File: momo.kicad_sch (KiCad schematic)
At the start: 98 parts, among them J1 USB C, SW1 MX_SW_HS, SW10 MX_SW_HS, SW11 MX_SW_HS, SW12 MX_SW_HS, SW13 MX_SW_HS, SW14 MX_SW_HS, SW15 MX_SW_HS, SW16 MX_SW_HS, SW17 MX_SW_HS, SW18 MX_SW_HS, SW19 MX_SW_HS, SW2 MX_SW_HS, SW20 MX_SW_HS, SW21 MX_SW_HS, SW22 MX_SW_HS, SW23 MX_SW_HS, SW24 MX_SW_HS, SW25 MX_SW_HS, SW26 MX_SW_HS, SW27 MX_SW_HS, SW28 MX_SW_HS, SW29 MX_SW_HS, SW3 MX_SW_HS, SW30 MX_SW_HS, SW31 MX_SW_HS, SW32 MX_SW_HS, SW33 MX_SW_HS, SW34 MX_SW_HS, SW35 MX_SW_HS, SW36 MX_SW_HS, SW37 MX_SW_HS, SW38 MX_SW_HS, SW39 MX_SW_HS, SW4 MX_SW_HS, SW40 MX_SW_HS, SW41 MX_SW_HS, SW42 MX_SW_HS, SW43 MX_SW_HS, SW44 MX_SW_HS, SW45 MX_SW_HS, SW46 MX_SW_HS, SW47 MX_SW_HS, SW48 MX_SW_HS, SW5 MX_SW_HS, SW6 MX_SW_HS, SW7 MX_SW_HS, SW8 MX_SW_HS, SW9 MX_SW_HS, U1 WeAct-RP2040-Pico

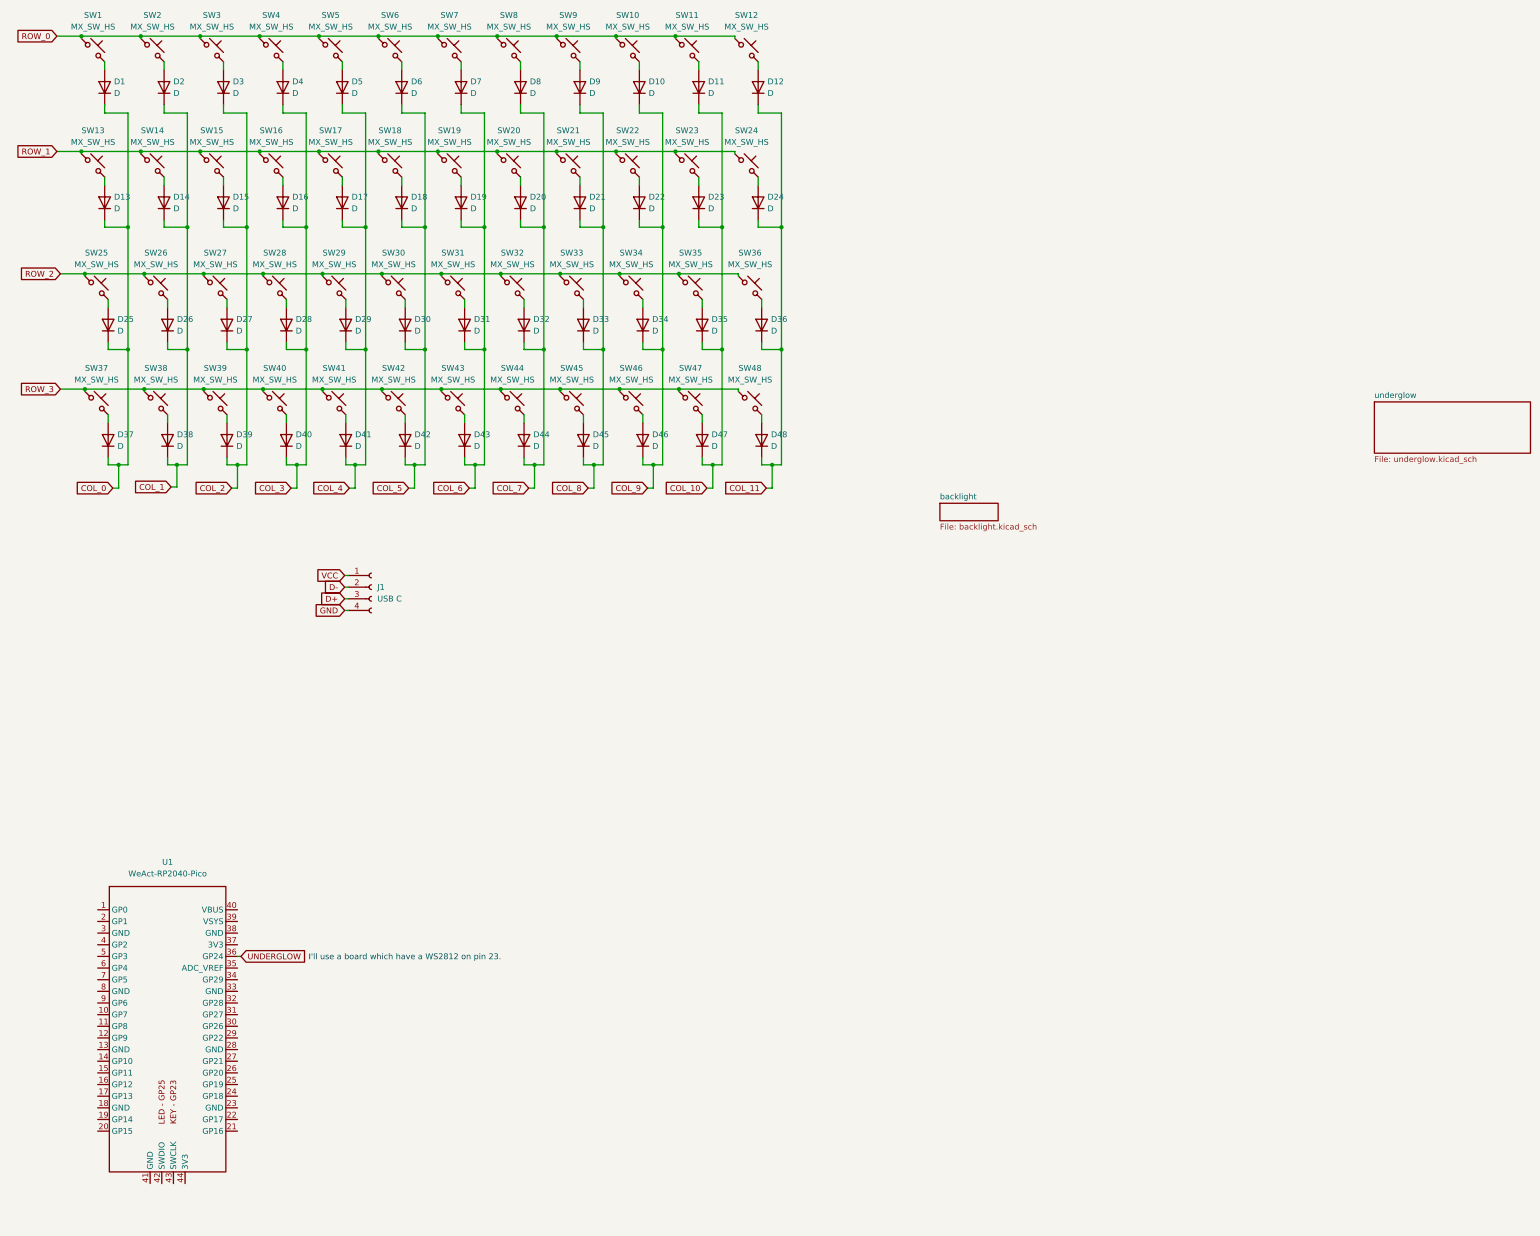
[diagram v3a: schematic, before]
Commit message: Added i2c pins
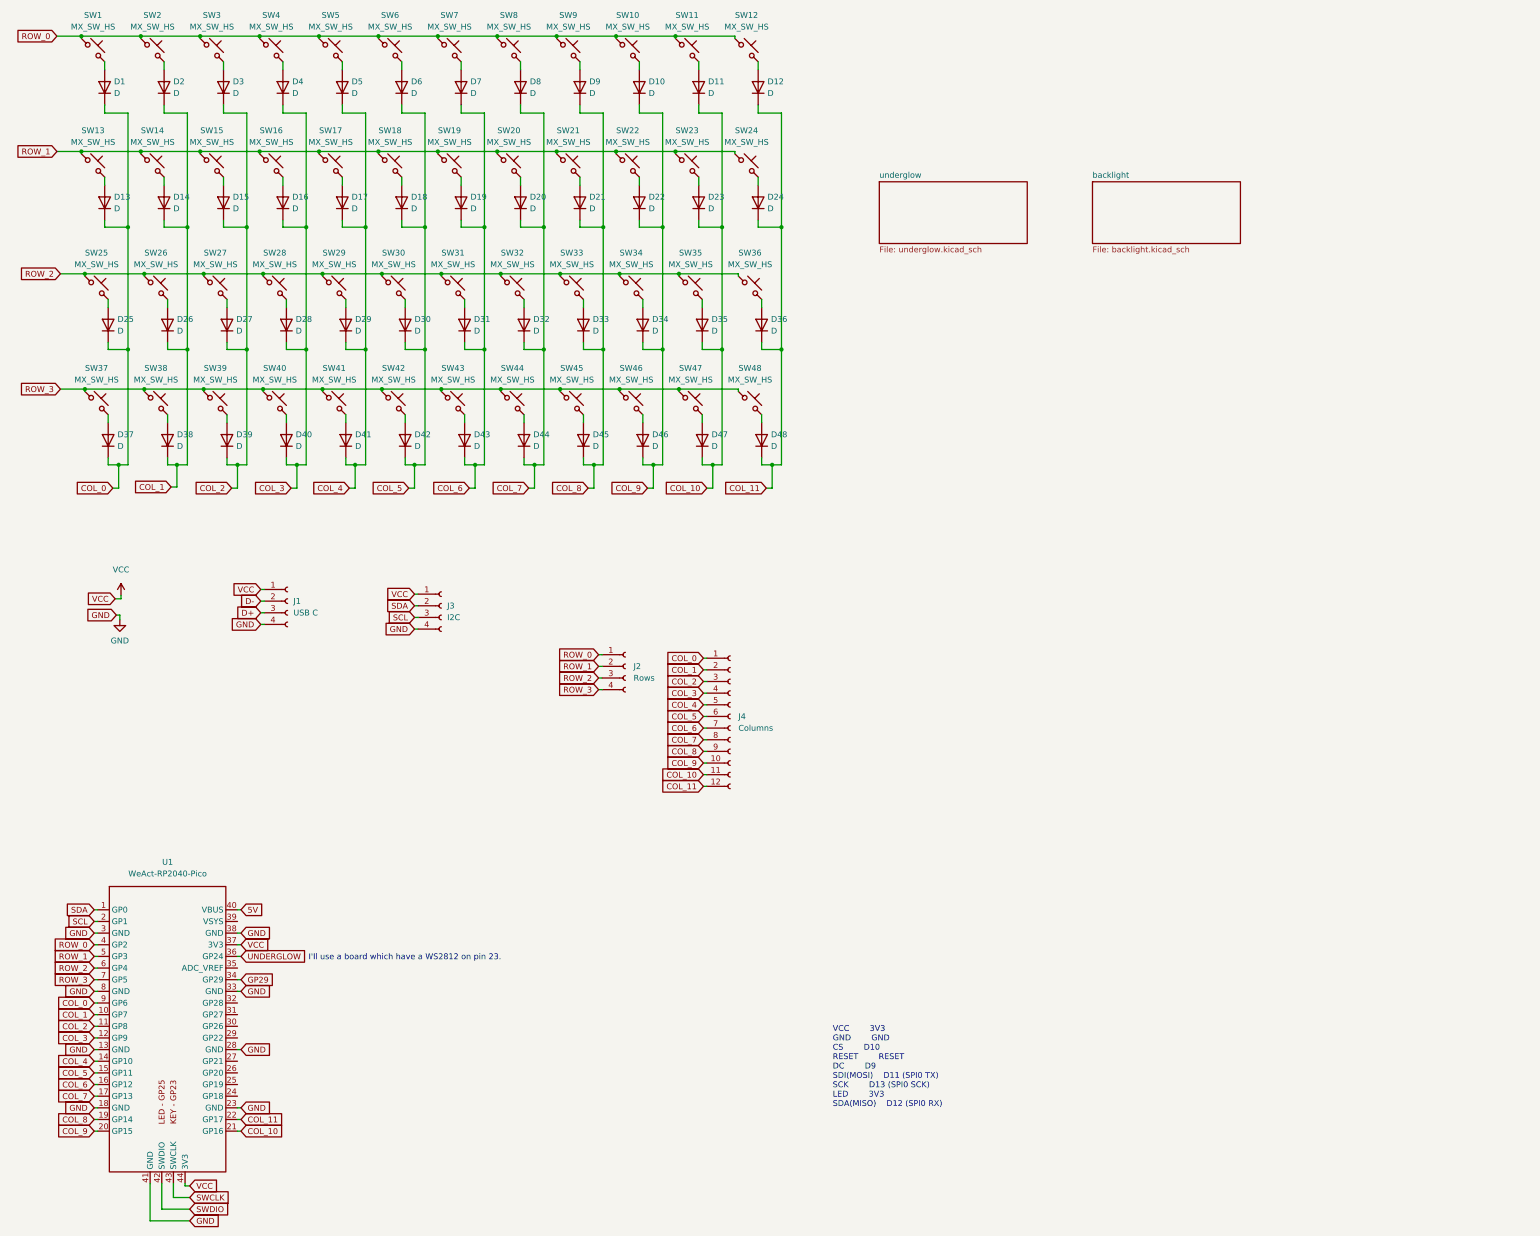
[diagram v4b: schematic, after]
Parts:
- added J2: Rows, Connector_PinHeader_2.54mm:PinHeader_1x04_P2.54mm_Vertical, symbol Connector:Conn_01x04_Female
- added J3: I2C, Connector_PinHeader_2.54mm:PinHeader_1x04_P2.54mm_Vertical, symbol Connector:Conn_01x04_Female
- added J4: Columns, Connector_PinHeader_2.54mm:PinHeader_1x12_P2.54mm_Vertical, symbol Connector:Conn_01x12_Female
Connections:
- net COL_0: now also U1.9 (GP6), J4.1 (Pin_1)
- net COL_1: now also U1.10 (GP7), J4.2 (Pin_2)
- net COL_10: now also U1.21 (GP16), J4.11 (Pin_11)
- net COL_11: now also U1.22 (GP17), J4.12 (Pin_12)
- net COL_2: now also U1.11 (GP8), J4.3 (Pin_3)
- net COL_3: now also U1.12 (GP9), J4.4 (Pin_4)
- net COL_4: now also U1.14 (GP10), J4.5 (Pin_5)
- net COL_5: now also U1.15 (GP11), J4.6 (Pin_6)
- net COL_6: now also U1.16 (GP12), J4.7 (Pin_7)
- net COL_7: now also U1.17 (GP13), J4.8 (Pin_8)
- net COL_8: now also U1.19 (GP14), J4.9 (Pin_9)
- net COL_9: now also U1.20 (GP15), J4.10 (Pin_10)
- net GND: now also U1.13 (GND), U1.18 (GND), U1.23 (GND), U1.28 (GND), U1.3 (GND), U1.33 (GND), U1.38 (GND), U1.41 (GND), U1.8 (GND), J3.4 (Pin_4)
- net ROW_0: now also U1.4 (GP2), J2.1 (Pin_1)
- net ROW_1: now also U1.5 (GP3), J2.2 (Pin_2)
- net ROW_2: now also U1.6 (GP4), J2.3 (Pin_3)
- net ROW_3: now also U1.7 (GP5), J2.4 (Pin_4)
- net VCC: now also U1.37 (3V3), U1.44 (3V3), J3.1 (Pin_1)
- net SDA: now reaches U1.1 (GP0)
- net SDA: now also J3.2 (Pin_2)
- net SCL: now reaches U1.2 (GP1)
- net SCL: now also J3.3 (Pin_3)
- net GP29: now reaches U1.34 (GP29)
- net 5V: now reaches U1.40 (VBUS)
- net SWDIO: now reaches U1.42 (SWDIO)
- net SWCLK: now reaches U1.43 (SWCLK)
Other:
- note added: "VCC 3V3 GND GND CS D10 RESET RESET DC D9 SDI(MOSI) D11 (SPI0 TX) SCK D13 (SPI0 SCK) LED 3V3 SDA(MISO) D12 (SPI0 RX)"
- moved on the sheet: J1

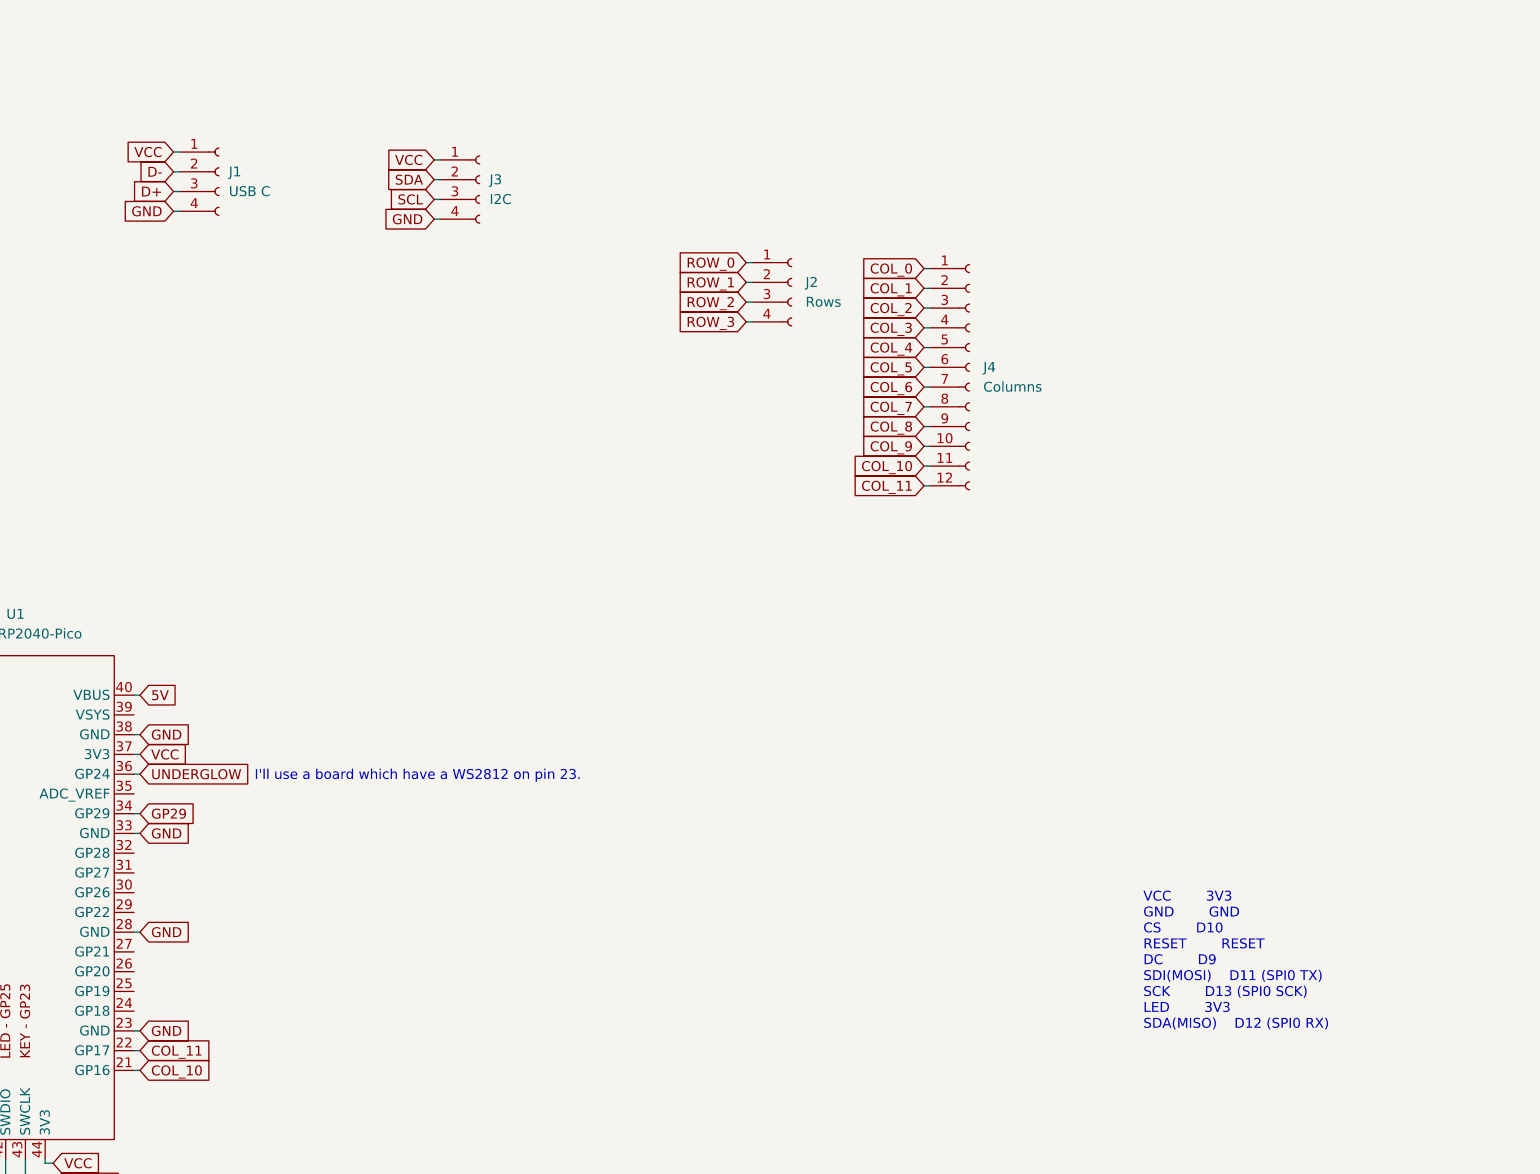
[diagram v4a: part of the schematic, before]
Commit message: Routed components
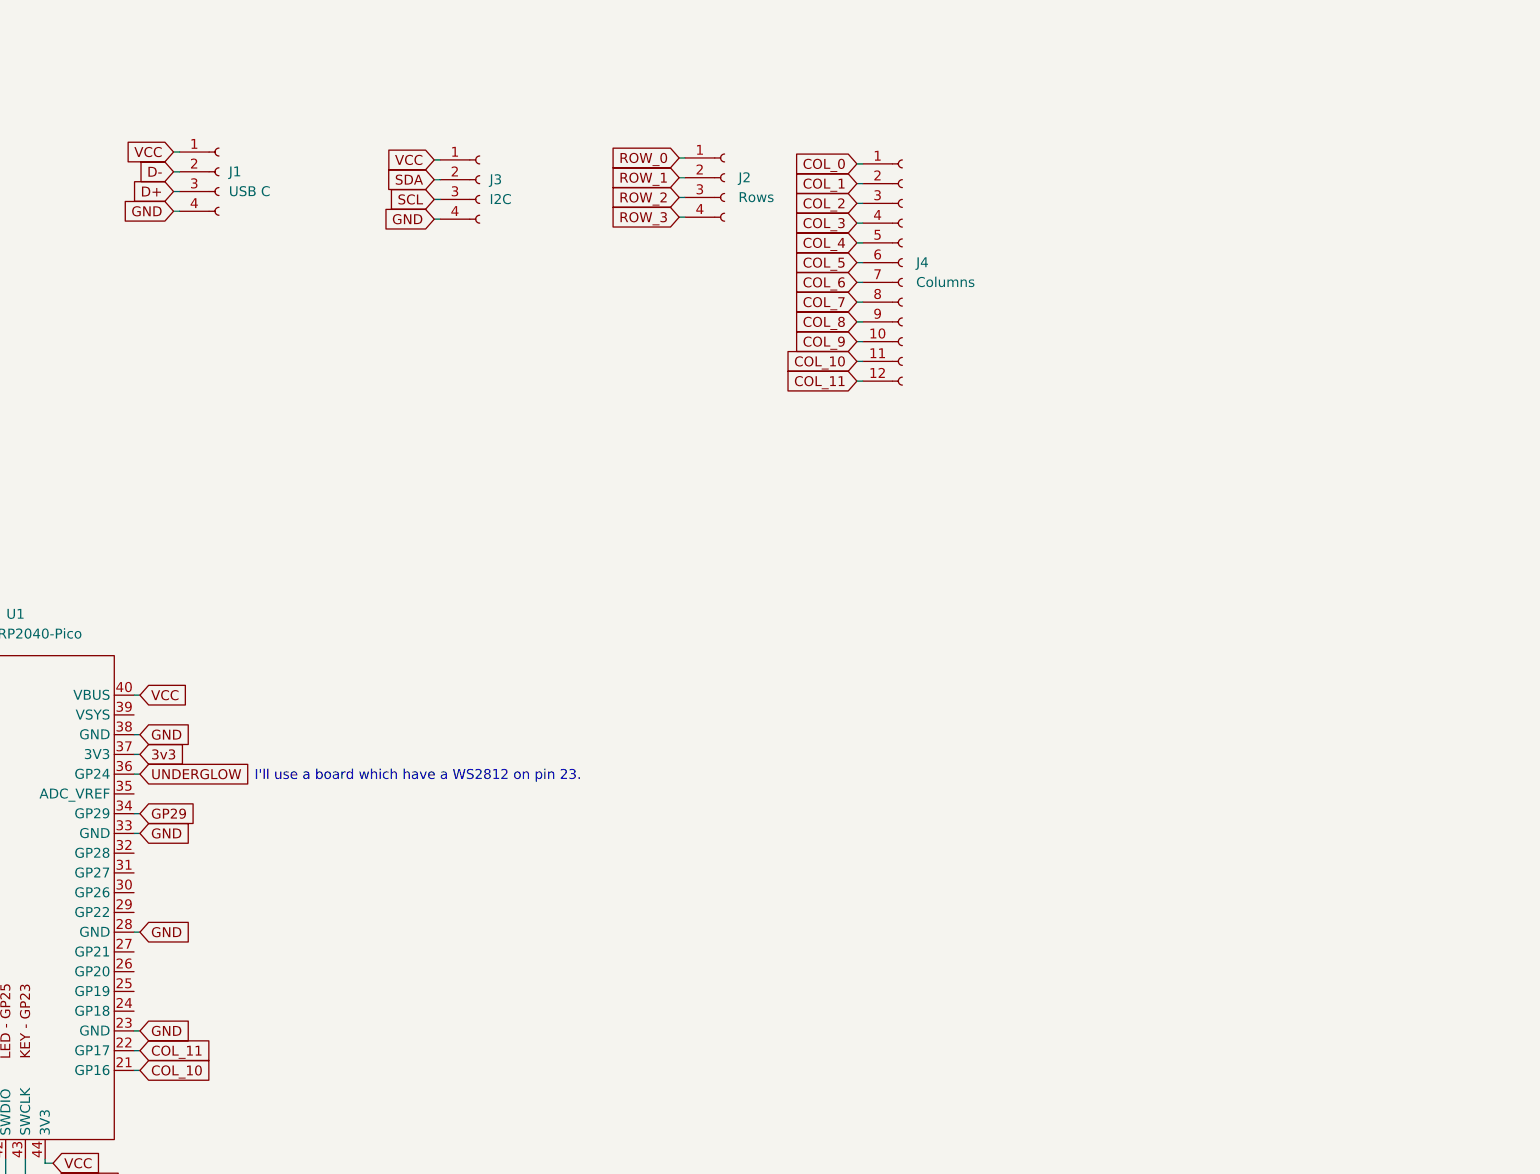
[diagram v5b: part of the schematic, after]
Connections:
- net 5V is gone; now on net VCC: U1.40 (VBUS)
- net VCC: no longer U1.37 (3V3)
- new net 3v3: U1.37 (3V3)
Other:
- note removed: "VCC 3V3 GND GND CS D10 RESET RESET DC D9 SDI(MOSI) D11 (SPI0 TX) SCK D13 (SPI0 SCK) LED 3V3 SDA(MISO) D12 (SPI0 RX)"
- moved on the sheet: J2, J4
